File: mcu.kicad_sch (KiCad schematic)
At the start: 18 parts, among them IC4 MIC39100-3.3WS, J1 USB_C_Receptacle_USB2.0_16P, SW1 SW_Push, U1 ESP32-S3-MINI-1U, U4 HLK-10M05

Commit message: added SD and minor fixes
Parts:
- added C14: 10u, symbol Device:C
- added C16: 100n, symbol Device:C
- added J11: Micro_SD_Card_Det_Hirose_DM3AT, Module:Maple_Mini, symbol Connector:Micro_SD_Card_Det_Hirose_DM3AT
- added R19, R20, R21, R22, R23: 10k, Resistor_SMD:R_0805_2012Metric, symbol Device:R
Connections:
- net +3.3V: now also C14.1, C16.1, J11.4 (VDD), R19.1, R20.1, R21.1, R22.1, R23.1
- net GND: now also C14.2, C16.2, J11.6 (VSS), J11.SH (SHIELD)
- net CMD: now reaches U1.34 (IO38)
- net CMD: now also J11.3 (CMD), R22.2
- net CLK_SD: now reaches U1.35 (IO39)
- net CLK_SD: now also J11.5 (CLK)
- net D0_SD: now reaches U1.36 (IO40)
- net D0_SD: now also J11.7 (DAT0), R23.2
- new net DAT1: J11.8 (DAT1), R21.2
- new net DAT2: J11.1 (DAT2), R19.2
- new net DAT3: J11.2 (DAT3/CD), R20.2
- no-connect marks 2 -> 4

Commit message: Footprint assignment
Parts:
- removed J11: Micro_SD_Card_Det_Hirose_DM3AT, Module:Maple_Mini, symbol Connector:Micro_SD_Card_Det_Hirose_DM3AT
- added J10: DM3AT-SF-PEJM5, SmartSupplyLib:DM3ATSFPEJM5, symbol SmartSupplyLib:DM3AT-SF-PEJM5
- C1, C14, C16, C3, C4, C5, C6: footprint (none) -> Capacitor_SMD:C_0805_2012Metric
- C2: footprint (none) -> Capacitor_SMD:C_1206_3216Metric
- C56: footprint Capacitor_SMD:C_0805_2012Metric -> Capacitor_SMD:C_1206_3216Metric
- FB1: footprint (none) -> SmartSupplyLib:fuse holder
- IC4: footprint SOT230P700X180-4N -> SmartSupplyLib:SOT230P700X180-4N
- R2, R5, R6, R7: footprint (none) -> Resistor_SMD:R_0805_2012Metric
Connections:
- net +3.3V: now also J10.4 (VDD)
- net CLK_SD: now also J10.5 (CLK)
- net CMD: now also J10.3 (CMD)
- net D0_SD: now also J10.7 (DAT0)
- net DAT1: now also J10.8 (DAT1)
- net DAT2: now also J10.1 (DAT2)
- net DAT3: now also J10.2 (CD/DAT3)
- net GND: now also J10.6 (VSS), J10.MP1, J10.MP2, J10.MP3, J10.MP4, J10.MP5, J10.MP6
- no-connect marks 4 -> 2

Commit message: MOV
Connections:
- net ZX2: now reaches U1.25 (IO21)
- net PGND renamed N
- net ZX renamed ZX1
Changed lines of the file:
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@@
 	(wire
 		(pts
+			(xy 60.96 39.37) (xy 64.77 39.37)
+		)
+		(stroke
+			(width 0)
+			(type default)
+		)
+	)
+	(wire
+		(pts
 			(xy 220.98 33.02) (xy 223.52 33.02)
 		)
@@
 		)
 	)
-	(label "ZX"
+	(label "ZX1"
 		(at 27.94 72.39 180)
 		(effects
@@
 		)
 	)
+	(label "ZX2"
+		(at 64.77 39.37 0)
+		(effects
+			(font
+				(size 1.27 1.27)
+			)
+			(justify left bottom)
+		)
+	)
 	(label "CMD"
 		(at 210.82 33.02 180)
@@
 			)
 		)
-		(property "Value" "PGND"
+		(property "Value" "N"
 			(at 16.51 147.574 0)
 			(show_name no)

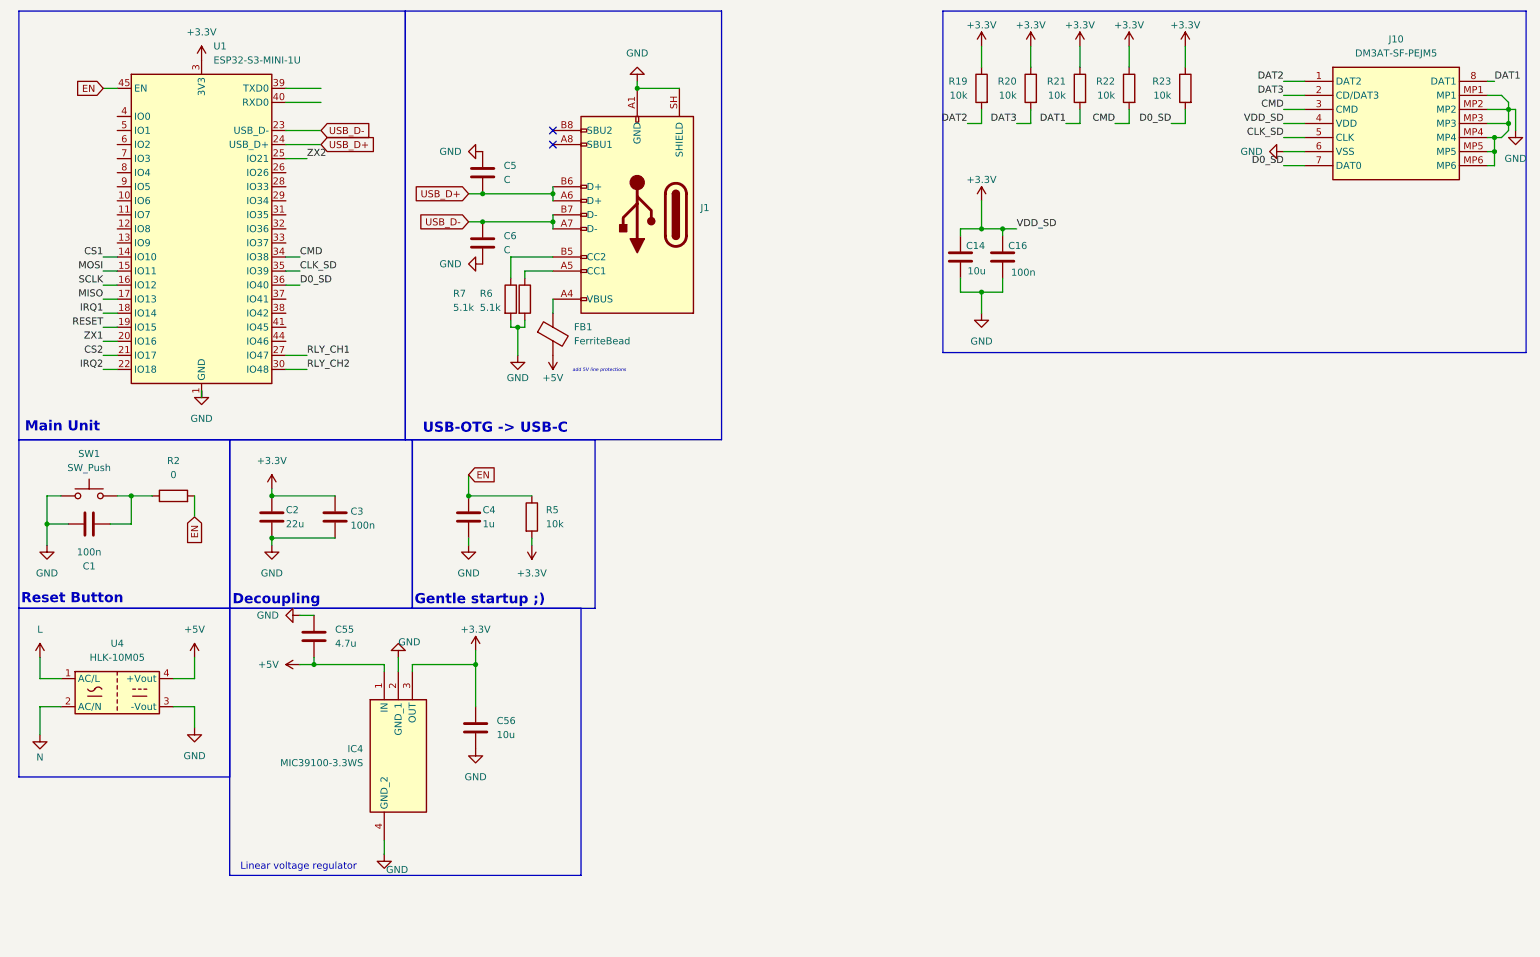
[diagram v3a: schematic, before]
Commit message: add usb 2.0 speed selector
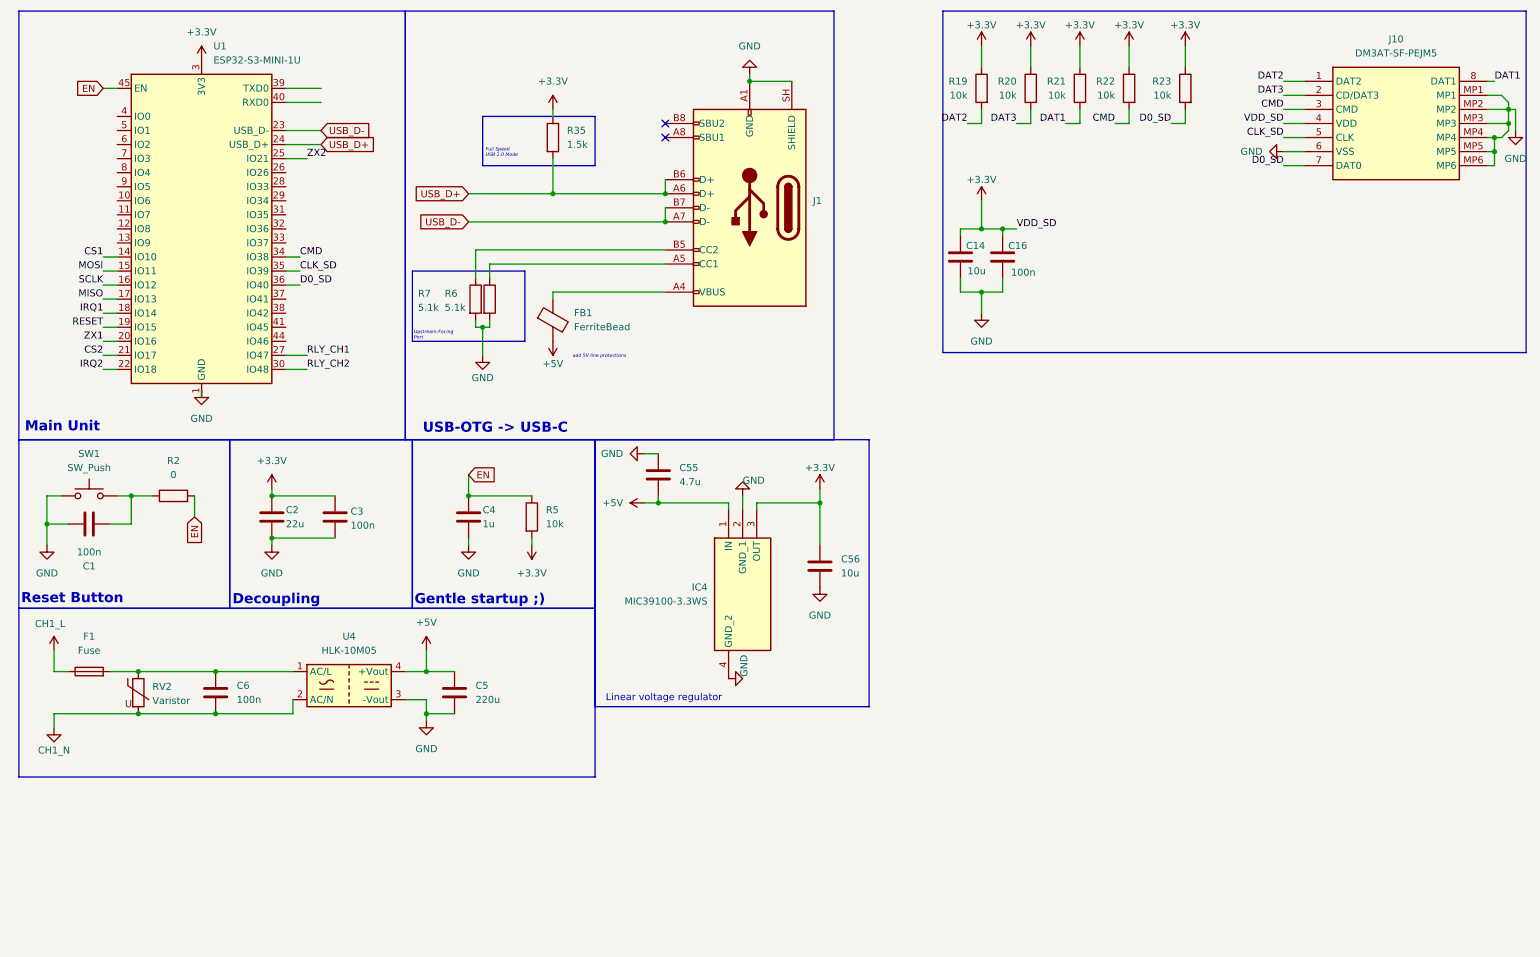
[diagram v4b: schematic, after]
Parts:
- added F1: Fuse, symbol Device:Fuse
- added R35: 1.5k, symbol Device:R
- added RV2: Varistor, symbol Device:Varistor
- C5: value C -> 220u; footprint Capacitor_SMD:C_0805_2012Metric -> (none)
- C6: value C -> 100n; footprint Capacitor_SMD:C_0805_2012Metric -> (none)
- J1: footprint Package_DFN_QFN:WQFN-16-1EP_3x3mm_P0.5mm_EP1.75x1.75mm -> Connector_USB:USB_C_Receptacle_Amphenol_124019772112A
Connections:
- net +3.3V: now also R35.1
- net +5V: now also C5.1
- net GND: now also C5.2; no longer C5.1, C6.2
- net USB_D+: now also R35.2; no longer C5.2
- net USB_D-: no longer C6.1
- net L: no longer names the net of U4.1 (AC/L)
- net L: now also C6.1, F1.2, RV2.1
- net N renamed CH1_N
- net CH1_N: now also C6.2, RV2.2
- new net CH1_L: F1.1
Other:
- note added: "Full Speed USB 2.0 Mode"
- note added: "Upstream-Facing Port"
- moved on the sheet: C55, C56, FB1, IC4, J1, R6, R7, U4

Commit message: add leds
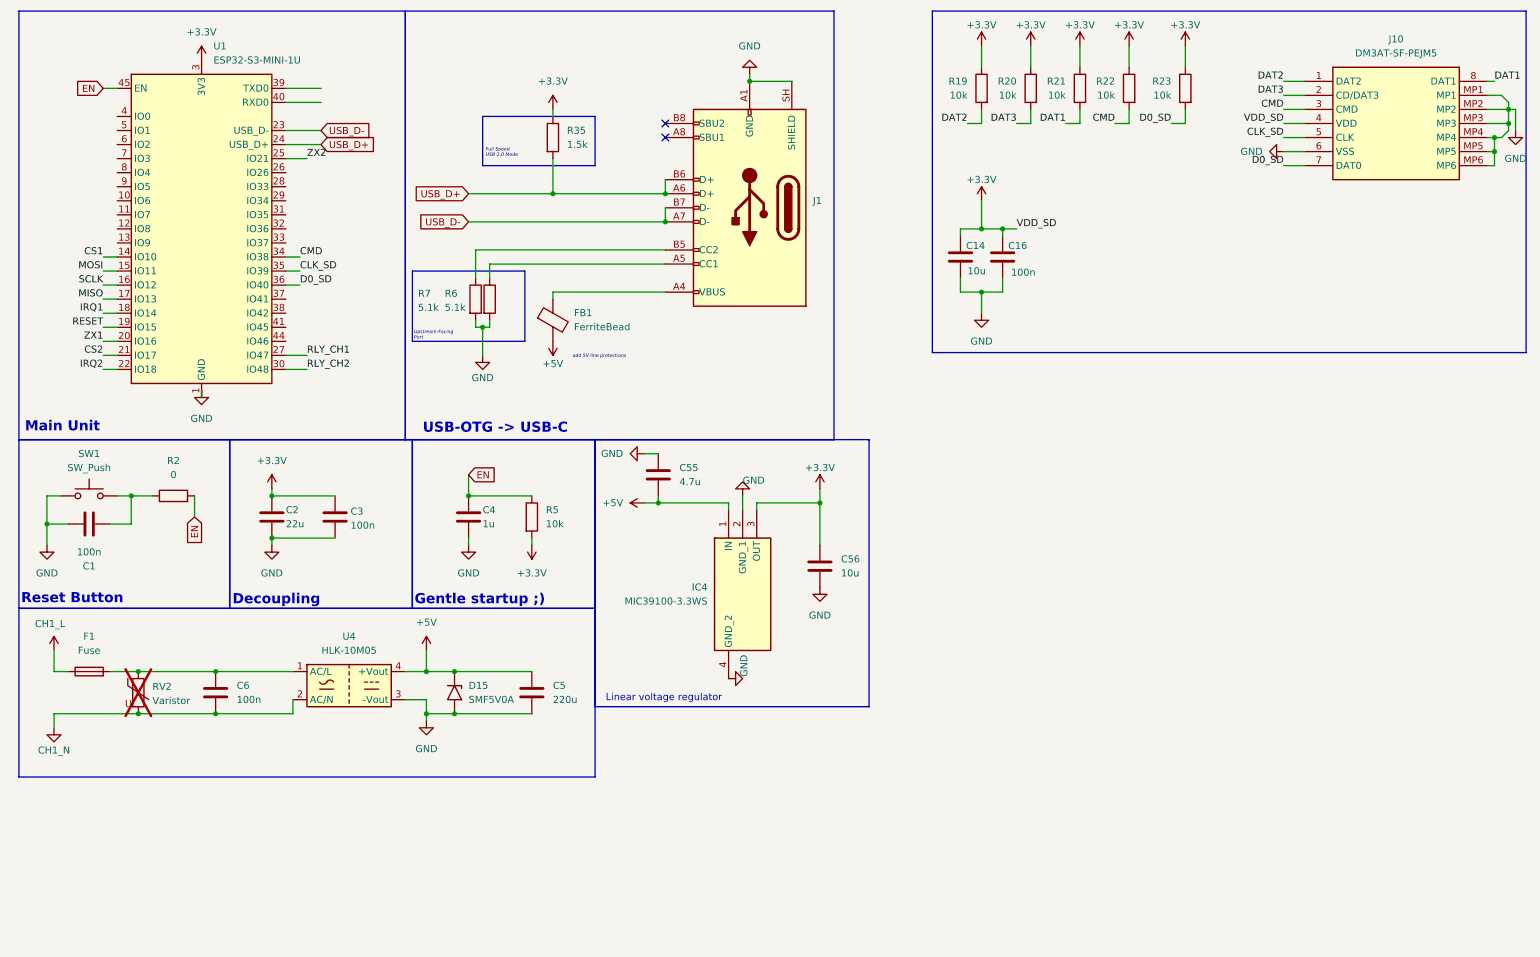
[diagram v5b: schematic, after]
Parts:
- added D15: SMF5V0A, Diode_SMD:D_SMF, symbol Diode:SMF5V0A
- C5: footprint (none) -> Capacitor_THT:C_Axial_L12.0mm_D6.5mm_P15.00mm_Horizontal
- C6: footprint (none) -> Capacitor_SMD:C_0805_2012Metric
- F1: footprint (none) -> SmartSupplyLib:fuse holder
- R35: footprint (none) -> Resistor_SMD:R_0805_2012Metric
- RV2: now not fitted
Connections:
- net +5V: now also D15.1 (A1)
- net GND: now also D15.2 (A2)
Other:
- moved on the sheet: C5
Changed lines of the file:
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@@
 	)
 	(rectangle
-		(start 179.705 12.7)
+		(start 177.8 12.7)
 		(end 285.115 74.422)
 		(stroke
@@
 	)
 	(junction
+		(at 91.44 132.08)
+		(diameter 0)
+		(color 0 0 0 0)
+	)
+	(junction
 		(at 186.69 52.07)
 		(diameter 0)
@@
 	)
 	(junction
+		(at 91.44 139.7)
+		(diameter 0)
+		(color 0 0 0 0)
+	)
+	(junction
 		(at 48.26 139.7)
 		(diameter 0)
@@
 	(wire
 		(pts
+			(xy 91.44 132.08) (xy 105.41 132.08)
+		)
+		(stroke
+			(width 0)
+			(type default)
+		)
+	)
+	(wire
+		(pts
 			(xy 241.3 25.4) (xy 245.11 25.4)
 		)
@@
 	(wire
 		(pts
+			(xy 91.44 139.7) (xy 105.41 139.7)
+		)
+		(stroke
+			(width 0)
+			(type default)
+		)
+	)
+	(wire
+		(pts
 			(xy 82.55 137.16) (xy 86.36 137.16)
 		)
@@
 			)
 		)
-		(property "Footprint" ""
+		(property "Footprint" "Capacitor_SMD:C_0805_2012Metric"
 			(at 49.2252 139.7 0)
 			(hide yes)
@@
 			)
 		)
-		(property "Footprint" ""
+		(property "Footprint" "Resistor_SMD:R_0805_2012Metric"
 			(at 107.442 35.56 90)
 			(hide yes)
@@
 	(symbol
 		(lib_id "Device:C")
-		(at 91.44 135.89 0)
+		(at 105.41 135.89 0)
 		(unit 1)
 		(body_style 1)
@@
 		(fields_autoplaced yes)
 		(property "Reference" "C5"
-			(at 95.25 134.6199 0)
+			(at 109.22 134.6199 0)
 			(show_name no)
 			(do_not_autoplace no)
@@
 		)
 		(property "Value" "220u"
-			(at 95.25 137.1599 0)
+			(at 109.22 137.1599 0)
 			(show_name no)
 			(do_not_autoplace no)
@@
 			)
 		)
-		(property "Footprint" ""
-			(at 92.4052 139.7 0)
+		(property "Footprint" "Capacitor_THT:C_Axial_L12.0mm_D6.5mm_P15.00mm_Horizontal"
+			(at 106.3752 139.7 0)
 			(hide yes)
 			(show_name no)
@@
 		)
 		(property "Datasheet" ""
-			(at 91.44 135.89 0)
+			(at 105.41 135.89 0)
 			(hide yes)
 			(show_name no)
@@
 		)
 		(property "Description" "Unpolarized capacitor"
-			(at 91.44 135.89 0)
+			(at 105.41 135.89 0)
 			(hide yes)
 			(show_name no)
@@
 		(on_board yes)
 		(in_pos_files yes)
-		(dnp no)
+		(dnp yes)
 		(fields_autoplaced yes)
 		(property "Reference" "RV2"
@@
 	)
 	(symbol
+		(lib_id "Diode:SMF5V0A")
+		(at 91.44 135.89 270)
+		(unit 1)
+		(body_style 1)
+		(exclude_from_sim no)
+		(in_bom yes)
+		(on_board yes)
+		(in_pos_files yes)
+		(dnp no)
+		(fields_autoplaced yes)
+		(property "Reference" "D15"
+			(at 93.98 134.6199 90)
+			(show_name no)
+			(do_not_autoplace no)
+			(effects
+				(font
+					(size 1.27 1.27)
+				)
+				(justify left)
+			)
+		)
+		(property "Value" "SMF5V0A"
+			(at 93.98 137.1599 90)
+			(show_name no)
+			(do_not_autoplace no)
+			(effects
+				(font
+					(size 1.27 1.27)
+				)
+				(justify left)
+			)
+		)
+		(property "Footprint" "Diode_SMD:D_SMF"
+			(at 86.36 135.89 0)
+			(hide yes)
+			(show_name no)
+			(do_not_autoplace no)
+			(effects
+				(font
+					(size 1.27 1.27)
+				)
+			)
+		)
+		(property "Datasheet" "https://www.vishay.com/doc?85881"
+			(at 91.44 134.62 0)
+			(hide yes)
+			(show_name no)
+			(do_not_autoplace no)
+			(effects
+				(font
+					(size 1.27 1.27)
+				)
+			)
+		)
+		(property "Description" "200W unidirectional Transil Transient Voltage Suppressor, 5Vrwm, SMF"
+			(at 91.44 135.89 0)
+			(hide yes)
+			(show_name no)
+			(do_not_autoplace no)
+			(effects
+				(font
+					(size 1.27 1.27)
+				)
+			)
+		)
+		(pin "1"
+		)
+		(pin "2"
+		)
+		(instances
+			(project "smart_supply"
+				(path "/487ef637-7a03-4925-80c1-798e0c6f0bbd/f9380e13-e191-4828-b42d-2cc7f479b711"
+					(reference "D15")
+					(unit 1)
+				)
+			)
+		)
+	)
+	(symbol
 		(lib_id "SmartSupplyLib:DM3AT-SF-PEJM5")
 		(at 245.11 25.4 0)
@@
 			)
 		)
-		(property "Footprint" ""
+		(property "Footprint" "SmartSupplyLib:fuse holder"
 			(at 25.4 133.858 90)
 			(hide yes)

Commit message: minimal change
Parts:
- added C17: 100n, Capacitor_SMD:C_0805_2012Metric, symbol Device:C
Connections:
- net +3.3V: now also C17.1
- net GND: now also C17.2
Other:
- moved on the sheet: C56
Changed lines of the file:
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@@
 	)
 	(junction
-		(at 157.48 101.6)
+		(at 153.67 101.6)
 		(diameter 0)
 		(color 0 0 0 0)
@@
 	)
 	(junction
+		(at 156.21 123.19)
+		(diameter 0)
+		(color 0 0 0 0)
+	)
+	(junction
 		(at 186.69 63.5)
 		(diameter 0)
@@
 	)
 	(junction
+		(at 157.48 101.6)
+		(diameter 0)
+		(color 0 0 0 0)
+	)
+	(junction
 		(at 281.94 33.02)
 		(diameter 0)
@@
 	(wire
 		(pts
+			(xy 153.67 123.19) (xy 153.67 116.84)
+		)
+		(stroke
+			(width 0)
+			(type default)
+		)
+	)
+	(wire
+		(pts
 			(xy 157.48 99.06) (xy 157.48 101.6)
 		)
@@
 	(wire
 		(pts
+			(xy 153.67 123.19) (xy 156.21 123.19)
+		)
+		(stroke
+			(width 0)
+			(type default)
+		)
+	)
+	(wire
+		(pts
 			(xy 280.67 27.94) (xy 281.94 29.21)
 		)
@@
 	(wire
 		(pts
+			(xy 158.75 101.6) (xy 158.75 109.22)
+		)
+		(stroke
+			(width 0)
+			(type default)
+		)
+	)
+	(wire
+		(pts
 			(xy 93.98 107.95) (xy 93.98 109.22)
 		)
@@
 	(wire
 		(pts
-			(xy 157.48 101.6) (xy 157.48 109.22)
+			(xy 153.67 101.6) (xy 153.67 109.22)
 		)
 		(stroke
@@
 	(wire
 		(pts
+			(xy 156.21 123.19) (xy 158.75 123.19)
+		)
+		(stroke
+			(width 0)
+			(type default)
+		)
+	)
+	(wire
+		(pts
 			(xy 144.78 24.13) (xy 144.78 25.4)
 		)
@@
 	(wire
 		(pts
+			(xy 157.48 101.6) (xy 158.75 101.6)
+		)
+		(stroke
+			(width 0)
+			(type default)
+		)
+	)
+	(wire
+		(pts
 			(xy 105.41 107.95) (xy 105.41 109.22)
 		)
@@
 	(wire
 		(pts
+			(xy 158.75 116.84) (xy 158.75 123.19)
+		)
+		(stroke
+			(width 0)
+			(type default)
+		)
+	)
+	(wire
+		(pts
 			(xy 241.3 35.56) (xy 245.11 35.56)
 		)
@@
 	)
 	(symbol
+		(lib_id "Device:C")
+		(at 158.75 113.03 0)
+		(unit 1)
+		(body_style 1)
+		(exclude_from_sim no)
+		(in_bom yes)
+		(on_board yes)
+		(in_pos_files yes)
+		(dnp no)
+		(property "Reference" "C17"
+			(at 159.766 110.998 0)
+			(show_name no)
+			(do_not_autoplace no)
+			(effects
+				(font
+					(size 1.27 1.27)
+				)
+				(justify left)
+			)
+		)
+		(property "Value" "100n"
+			(at 159.766 116.078 0)
+			(show_name no)
+			(do_not_autoplace no)
+			(effects
+				(font
+					(size 1.27 1.27)
+				)
+				(justify left)
+			)
+		)
+		(property "Footprint" "Capacitor_SMD:C_0805_2012Metric"
+			(at 159.7152 116.84 0)
+			(hide yes)
+			(show_name no)
+			(do_not_autoplace no)
+			(effects
+				(font
+					(size 1.27 1.27)
+				)
+			)
+		)
+		(property "Datasheet" ""
+			(at 158.75 113.03 0)
+			(hide yes)
+			(show_name no)
+			(do_not_autoplace no)
+			(effects
+				(font
+					(size 1.27 1.27)
+				)
+			)
+		)
+		(property "Description" "Unpolarized capacitor"
+			(at 158.75 113.03 0)
+			(hide yes)
+			(show_name no)
+			(do_not_autoplace no)
+			(effects
+				(font
+					(size 1.27 1.27)
+				)
+			)
+		)
+		(pin "2"
+		)
+		(pin "1"
+		)
+		(instances
+			(project "smart_supply"
+				(path "/487ef637-7a03-4925-80c1-798e0c6f0bbd/f9380e13-e191-4828-b42d-2cc7f479b711"
+					(reference "C17")
+					(unit 1)
+				)
+			)
+		)
+	)
+	(symbol
 		(lib_id "power:+3.3V")
 		(at 19.05 128.27 0)
@@
 	(symbol
 		(lib_id "power:GND")
-		(at 157.48 116.84 0)
+		(at 156.21 123.19 0)
 		(unit 1)
 		(body_style 1)
@@
 		(fields_autoplaced yes)
 		(property "Reference" "#PWR0113"
-			(at 157.48 123.19 0)
+			(at 156.21 129.54 0)
 			(hide yes)
 			(show_name no)
@@
 		)
 		(property "Value" "GND"
-			(at 157.48 121.92 0)
+			(at 156.21 128.27 0)
 			(show_name no)
 			(do_not_autoplace no)
@@
 		)
 		(property "Footprint" "DDPAK3_MC_MCH"
-			(at 157.48 116.84 0)
+			(at 156.21 123.19 0)
 			(hide yes)
 			(show_name no)
@@
 		)
 		(property "Datasheet" ""
-			(at 157.48 116.84 0)
+			(at 156.21 123.19 0)
 			(hide yes)
 			(show_name no)
@@
 		)
 		(property "Description" "Power symbol creates a global label with name \"GND\" , ground"
-			(at 157.48 116.84 0)
+			(at 156.21 123.19 0)
 			(hide yes)
 			(show_name no)
@@
 	(symbol
 		(lib_id "Device:C")
-		(at 157.48 113.03 0)
+		(at 153.67 113.03 0)
 		(unit 1)
 		(body_style 1)
@@
 		(in_pos_files yes)
 		(dnp no)
-		(fields_autoplaced yes)
 		(property "Reference" "C56"
-			(at 161.29 111.7599 0)
+			(at 153.924 110.998 0)
 			(show_name no)
 			(do_not_autoplace no)
@@
 		)
 		(property "Value" "10u"
-			(at 161.29 114.2999 0)
+			(at 153.924 115.316 0)
 			(show_name no)
 			(do_not_autoplace no)
@@
 		)
 		(property "Footprint" "Capacitor_SMD:C_1206_3216Metric"
-			(at 158.4452 116.84 0)
+			(at 154.6352 116.84 0)
 			(hide yes)
 			(show_name no)
@@
 		)
 		(property "Datasheet" ""
-			(at 157.48 113.03 0)
+			(at 153.67 113.03 0)
 			(hide yes)
 			(show_name no)
@@
 		)
 		(property "Description" "Unpolarized capacitor"
-			(at 157.48 113.03 0)
+			(at 153.67 113.03 0)
 			(hide yes)
 			(show_name no)
